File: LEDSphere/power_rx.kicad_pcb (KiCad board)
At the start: 2 copper layers, 140 x 140 mm, 47 parts, among them U10 DRV5032FCDBZR, U3 TPS54202HDDCR, U4 TPS54202HDDCR

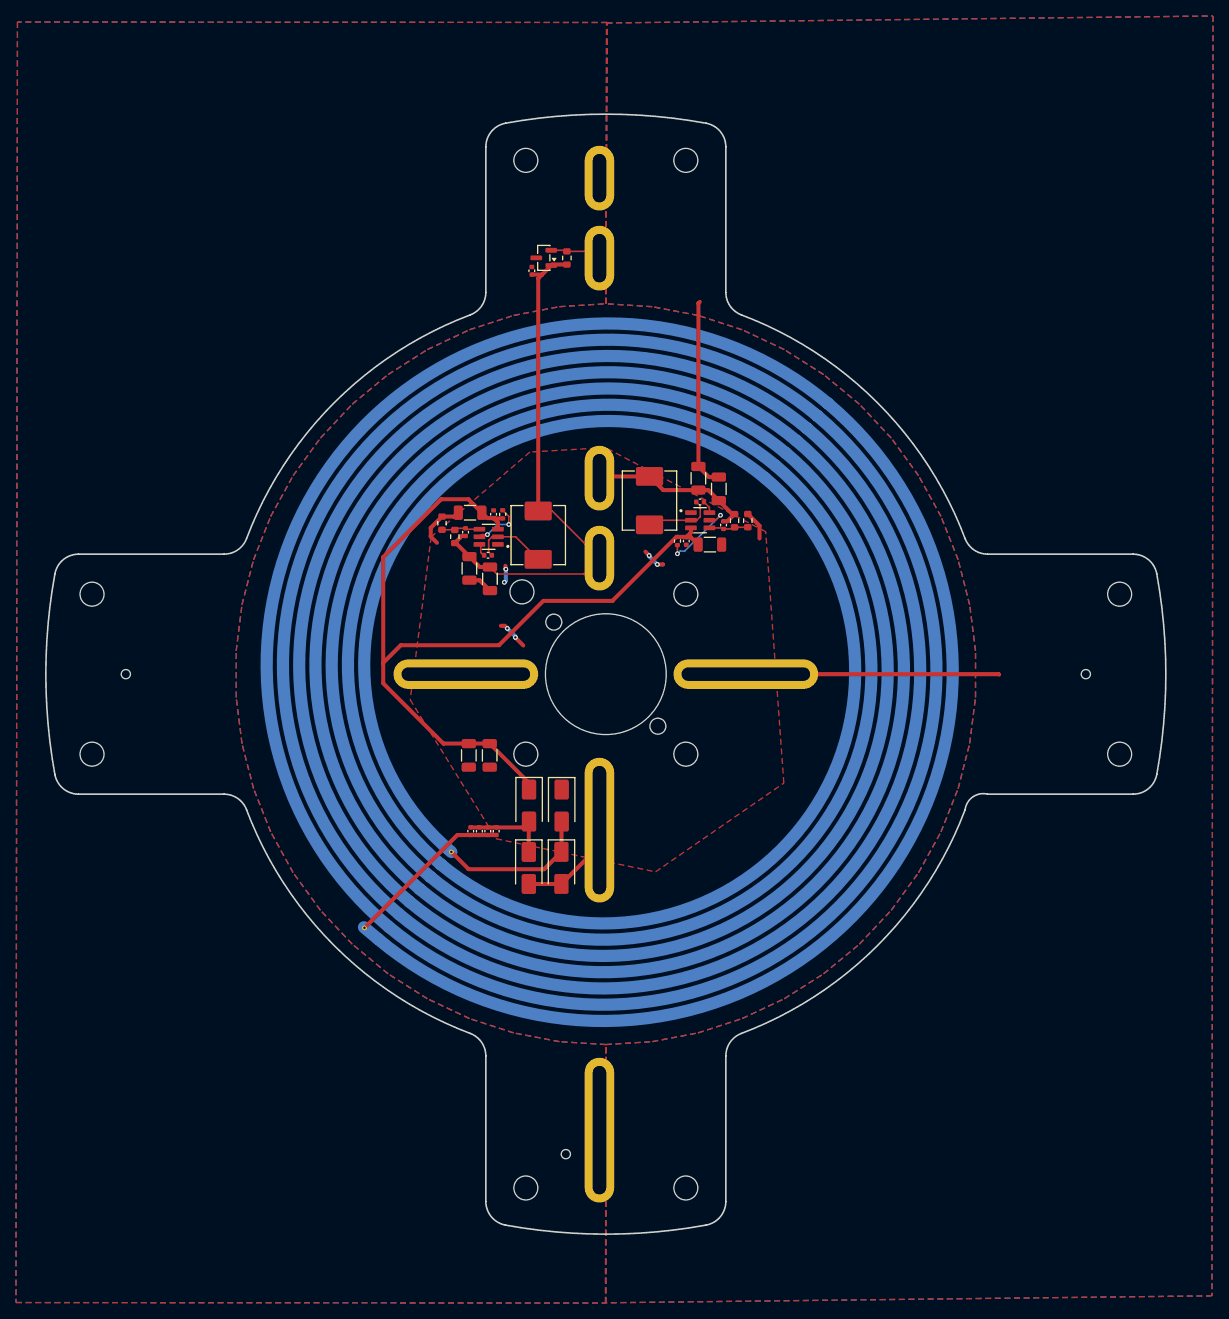
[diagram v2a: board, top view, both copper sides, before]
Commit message: power rx layout change
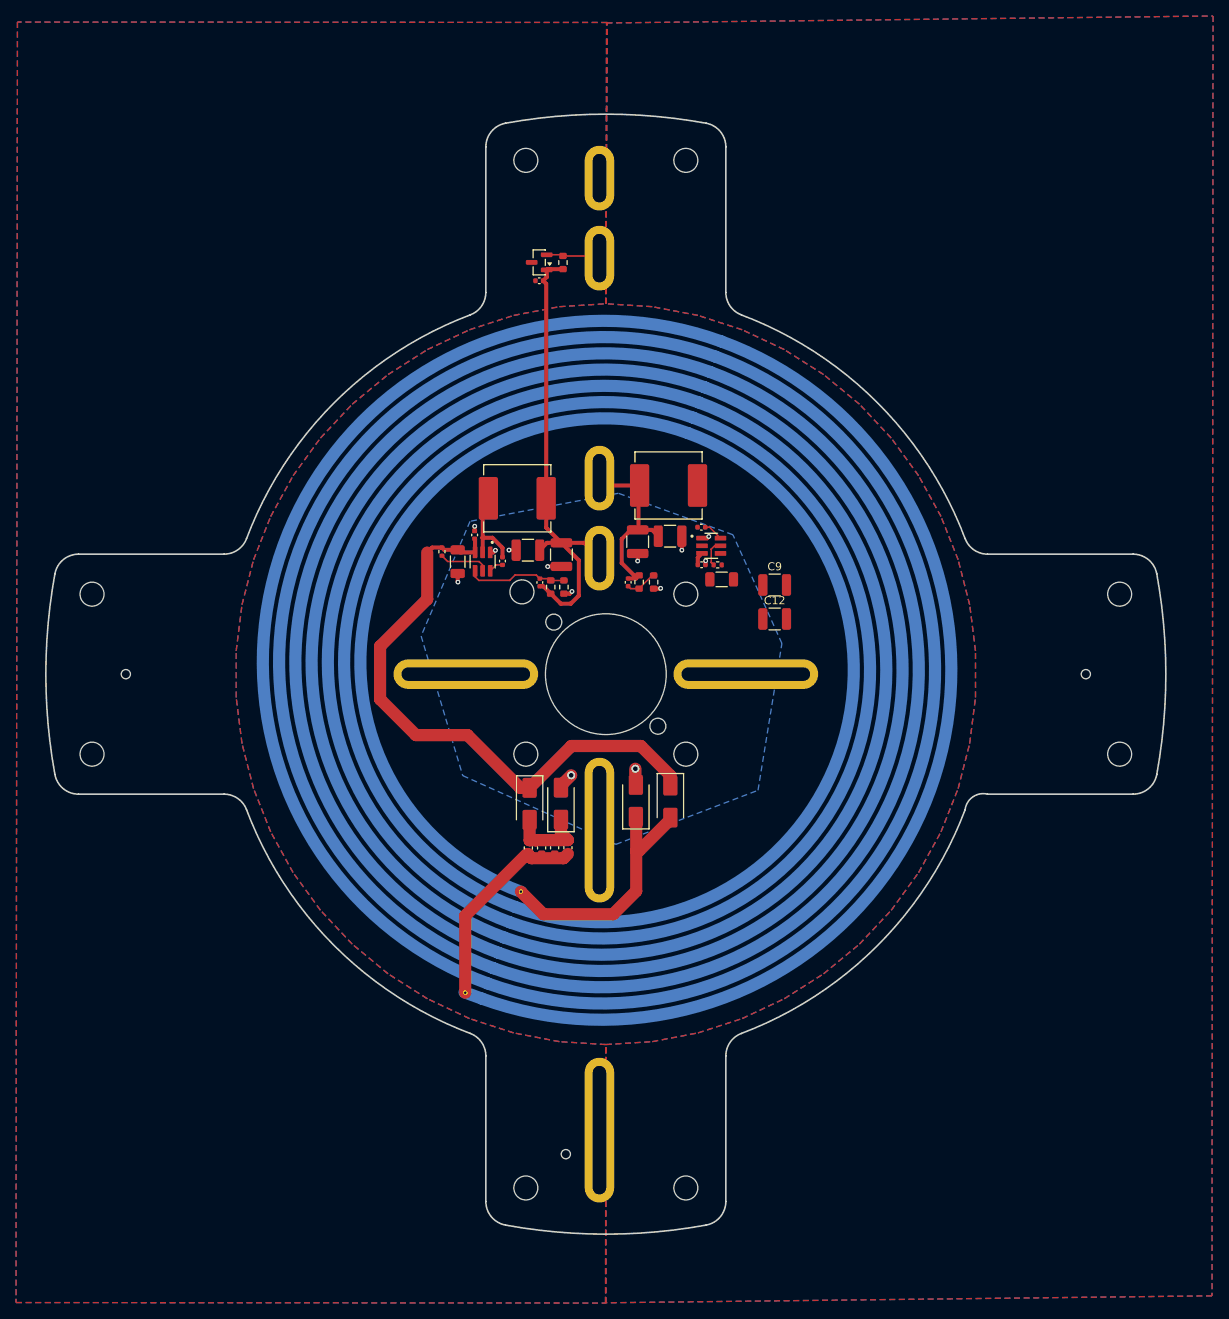
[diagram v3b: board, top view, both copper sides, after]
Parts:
- C12, C9: value 22µF, 25V -> 22uF; footprint Capacitor_SMD:C_1206_3216Metric -> Capacitor_SMD:C_1210_3225Metric
- C13, C14, C15, C16: footprint Capacitor_SMD:C_1206_3216Metric -> Capacitor_SMD:C_1210_3225Metric
- C5, C6, C7, C8: footprint Capacitor_SMD:C_0402_1005Metric -> Capacitor_SMD:C_0603_1608Metric
- L2, L3: footprint Inductor_SMD:L_Abracon_ASPI-0630LR -> Inductor_SMD:L_Vishay_IHLP-3232
- moved C12 41.9 mm to (115.6, 97.4), turned to 0 degrees
- moved C9 41.5 mm to (115.6, 93.1), turned to 0 degrees
- moved R4 17.2 mm to (89.2, 93.4), turned to 90 degrees
- moved R5 14.2 mm to (98.7, 92.8)
- moved R6 14.1 mm to (100.5, 92.8), turned to 90 degrees
- moved C18 13.9 mm to (97.3, 92.8)
- moved D3 13.6 mm to (102.6, 120.2)
- moved R3 13.6 mm to (87.6, 93.4)
- moved D4 12.5 mm to (98.2, 120.1), turned to 90 degrees
- moved C5 12.3 mm to (89.8, 126.0)
- moved C17 11.2 mm to (86.2, 92.8)
- moved C14 11.0 mm to (98.5, 87.7), turned to 90 degrees
- moved C15 9.43 mm to (88.9, 89.3)
- moved D2 8.99 mm to (88.9, 120.5), turned to 90 degrees
- moved R1 8.92 mm to (74.0, 89.0), turned to 90 degrees
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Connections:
- C12 pad 1: /U_unreg -> GND
- C12 pad 2: GND -> /U_unreg
- C9 pad 1: /U_unreg -> GND
- C9 pad 2: GND -> /U_unreg
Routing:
- net GND: track 90.4 -> 15.4 mm, vias 6 -> 13
- net /U_unreg: track 108.2 -> 76.5 mm
- net /coil1: track 19.3 -> 32.2 mm
- net Net-(U4-SW): track 8.81 -> 0.00 mm
- net Net-(U3-FB): track 4.82 -> 12.6 mm
- net +3.3V: track 66.9 -> 59.7 mm
- net Net-(U4-EN): track 10.1 -> 3.42 mm, vias 2 -> 0
- net /coil2: track 21.3 -> 26.0 mm
- net +5V: track 20.7 -> 23.8 mm
- net Net-(U3-SW): track 9.59 -> 11.2 mm
- net Net-(D1-A): track 11.4 -> 10.3 mm
- net Net-(U4-FB): track 4.95 -> 3.99 mm
- net Net-(U4-BOOT): track 1.63 -> 2.47 mm
- net Net-(U3-EN): track 6.41 -> 6.30 mm, vias 2 -> 0

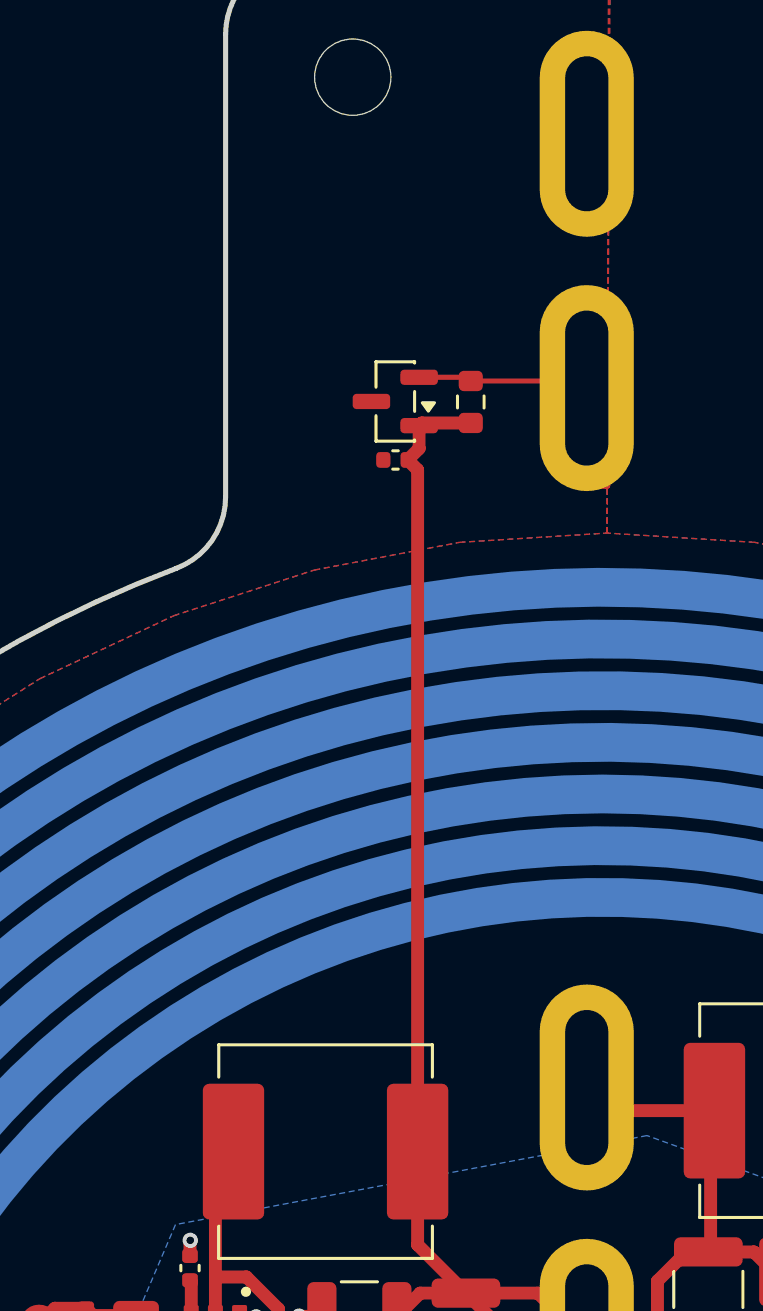
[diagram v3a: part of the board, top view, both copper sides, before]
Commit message: change hall effect sensor
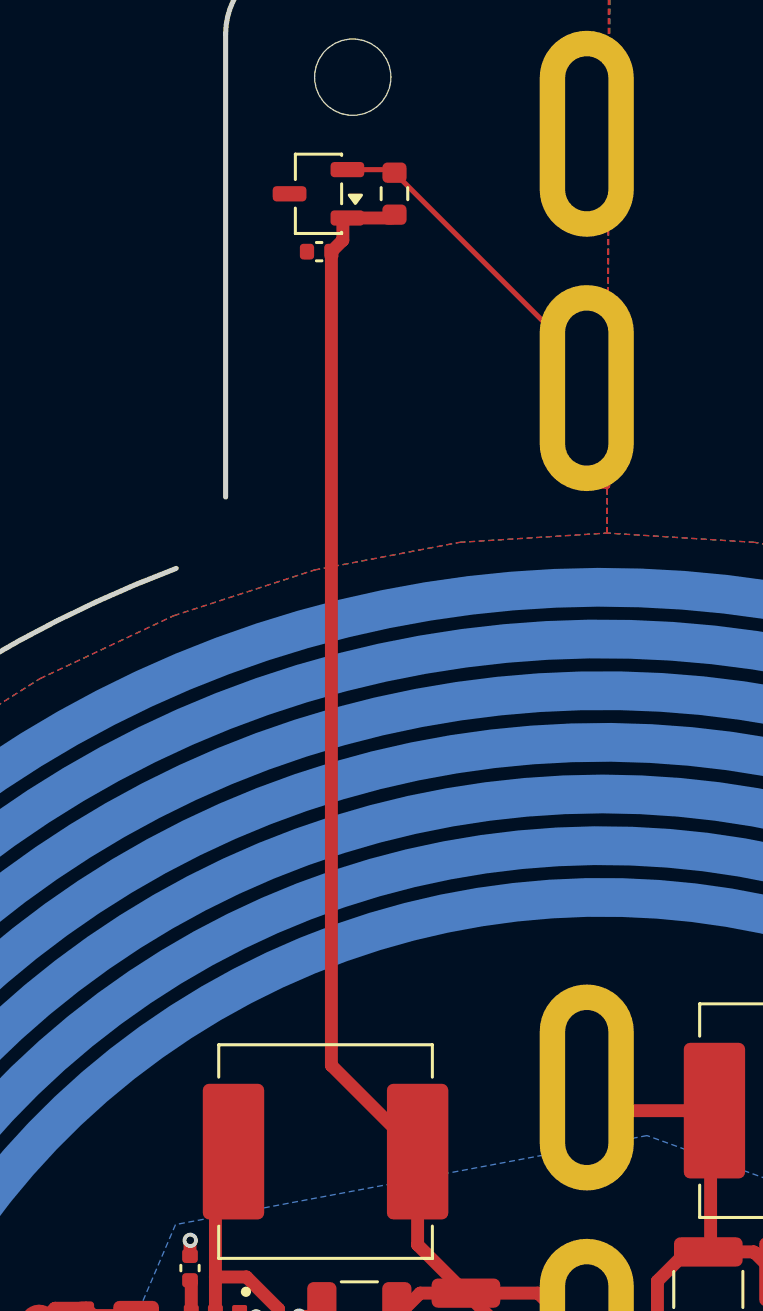
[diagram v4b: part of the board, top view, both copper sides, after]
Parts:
- removed U10: DRV5032FCDBZR, Package_TO_SOT_SMD:SOT-23
- added U114: DRV5033FAQDBZR, Package_TO_SOT_SMD:SOT-23-3, F.Cu at (83.1, 44.6)
- R7: value 20k -> 10k
- moved R7 8.72 mm to (86.1, 44.6)
- moved C19 8.72 mm to (83.2, 46.9)
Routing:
- net +3.3V: track 59.7 -> 69.0 mm
- net Hall: track 11.6 -> 18.5 mm

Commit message: wrap up rx
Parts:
- moved C12 39.4 mm to (78.3, 110.1), turned to 180 degrees
- moved C9 19.6 mm to (110.7, 112.1), turned to -90 degrees
- moved C14 12.8 mm to (111.2, 89.2)
- moved R5 12.3 mm to (110.9, 93.8)
- moved R6 12.3 mm to (112.7, 93.8)
- moved C18 12.3 mm to (109.5, 93.8)
- moved R2 11.5 mm to (97.0, 91.2), turned to -90 degrees
- moved C2 10.4 mm to (98.8, 89.9), turned to -90 degrees
- moved C4 7.47 mm to (100.3, 86.4), turned to -90 degrees
- moved U4 5.99 mm to (101.8, 89.7), turned to -90 degrees
- moved C16 4.83 mm to (107.1, 88.5), turned to 0 degrees
- moved C11 4.46 mm to (104.2, 89.8), turned to -90 degrees
- moved L3 3.43 mm to (105.3, 82.4), turned to 0 degrees
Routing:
- net /U_unreg: track 76.5 -> 141.3 mm
- net +5V: track 23.8 -> 35.3 mm
- net Net-(U4-SW): track 0.00 -> 9.33 mm
- net Net-(U4-EN): track 3.42 -> 12.4 mm, vias 0 -> 2
- net Net-(U4-FB): track 3.99 -> 10.7 mm
- net GND: track 15.4 -> 12.7 mm, vias 13 -> 10
- net +3.3V: track 69.0 -> 71.2 mm
- net Net-(U4-BOOT): track 2.47 -> 1.66 mm

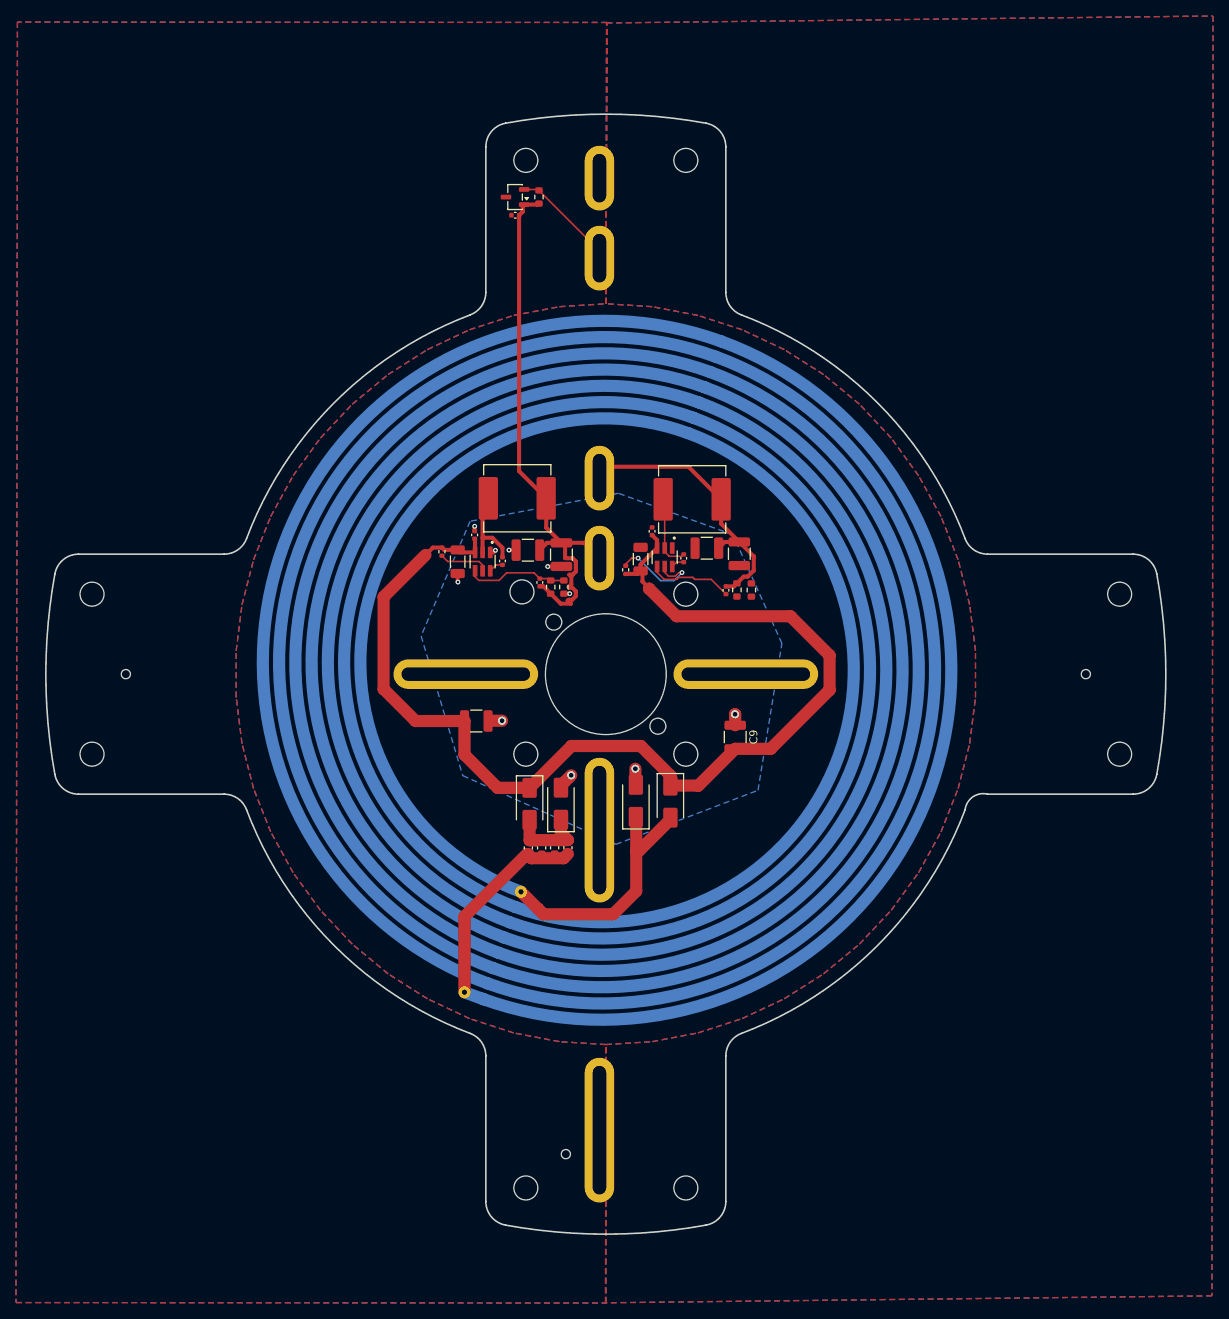
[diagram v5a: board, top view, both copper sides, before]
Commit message: cut gnd plane
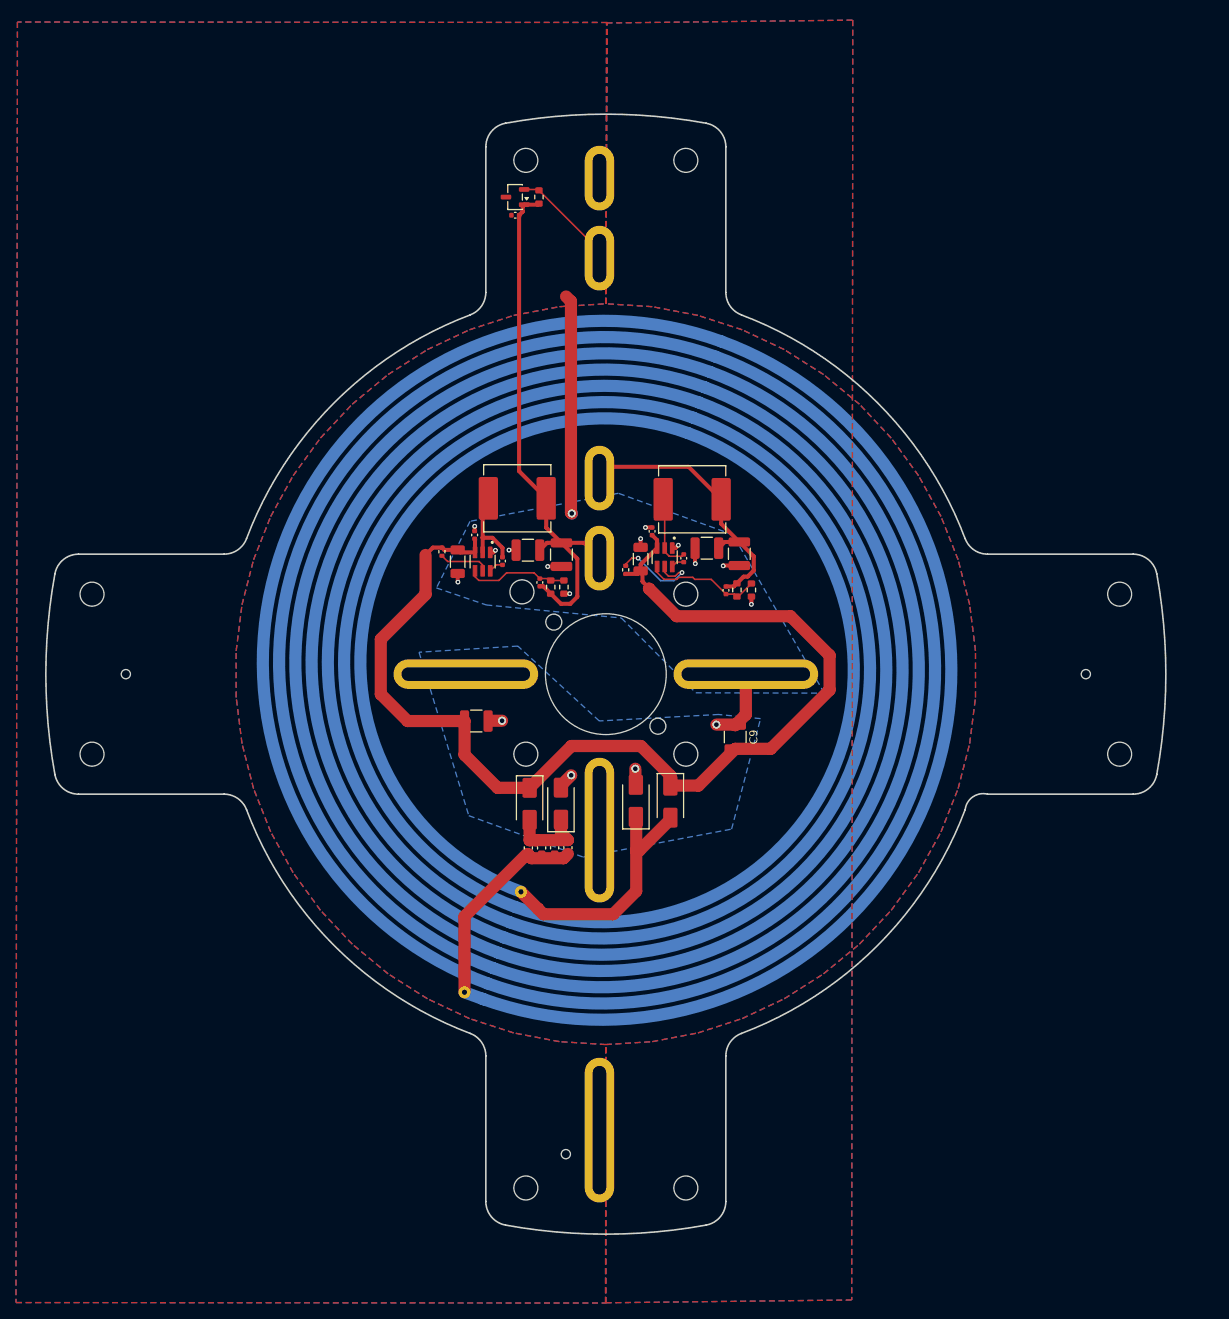
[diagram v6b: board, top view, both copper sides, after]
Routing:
- net GND: track 12.7 -> 55.8 mm, vias 10 -> 17
- net Net-(U4-FB): track 10.7 -> 14.7 mm
- net +3.3V: track 71.2 -> 68.8 mm
- net /U_unreg: track 141.3 -> 142.2 mm
